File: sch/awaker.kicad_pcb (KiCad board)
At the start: 2 copper layers, 35 parts, among them P1 CONN_01X03, P2 CONN_01X07, P3 uart, P4 swd, P5 CONN_01X06, P6 speaker, P7 pow_led, P8 power, P9 CONN_01X07, Q1 Q_NMOS_GDS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

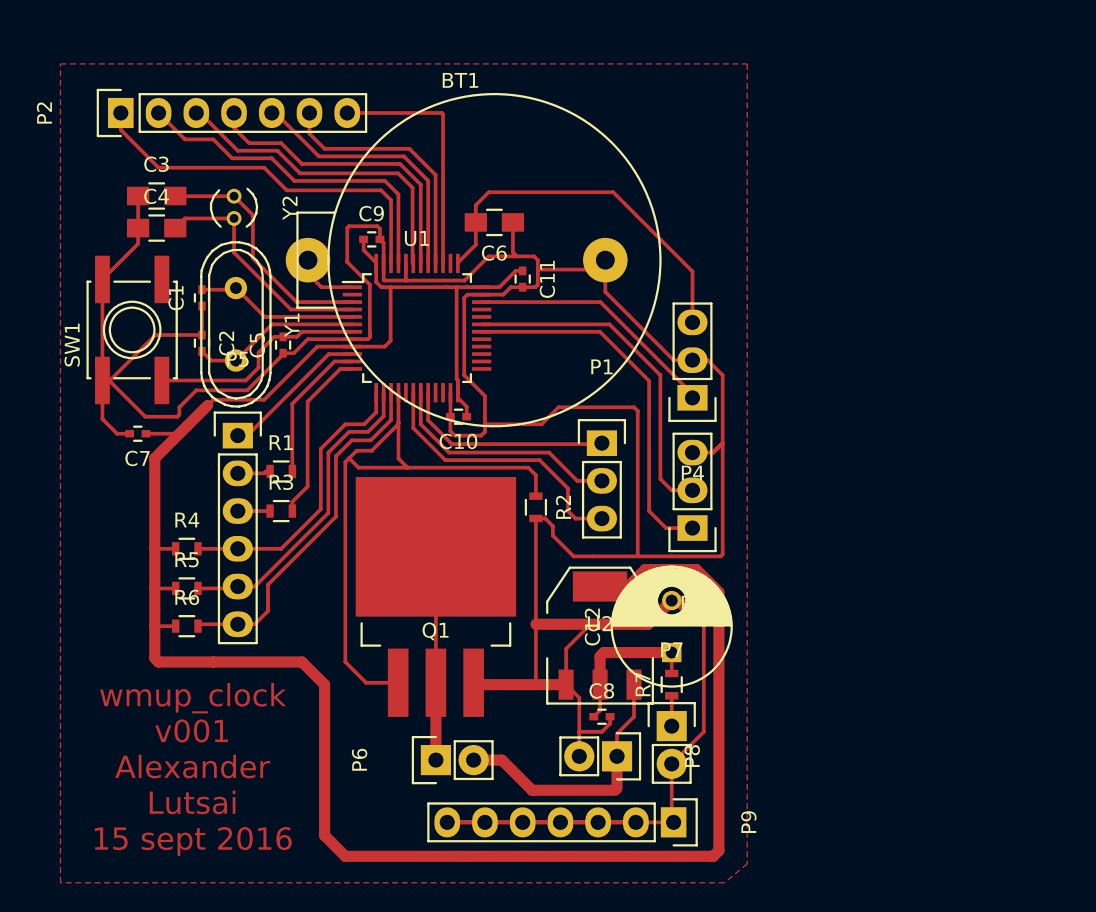
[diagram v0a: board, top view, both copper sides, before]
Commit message: reset. New board.
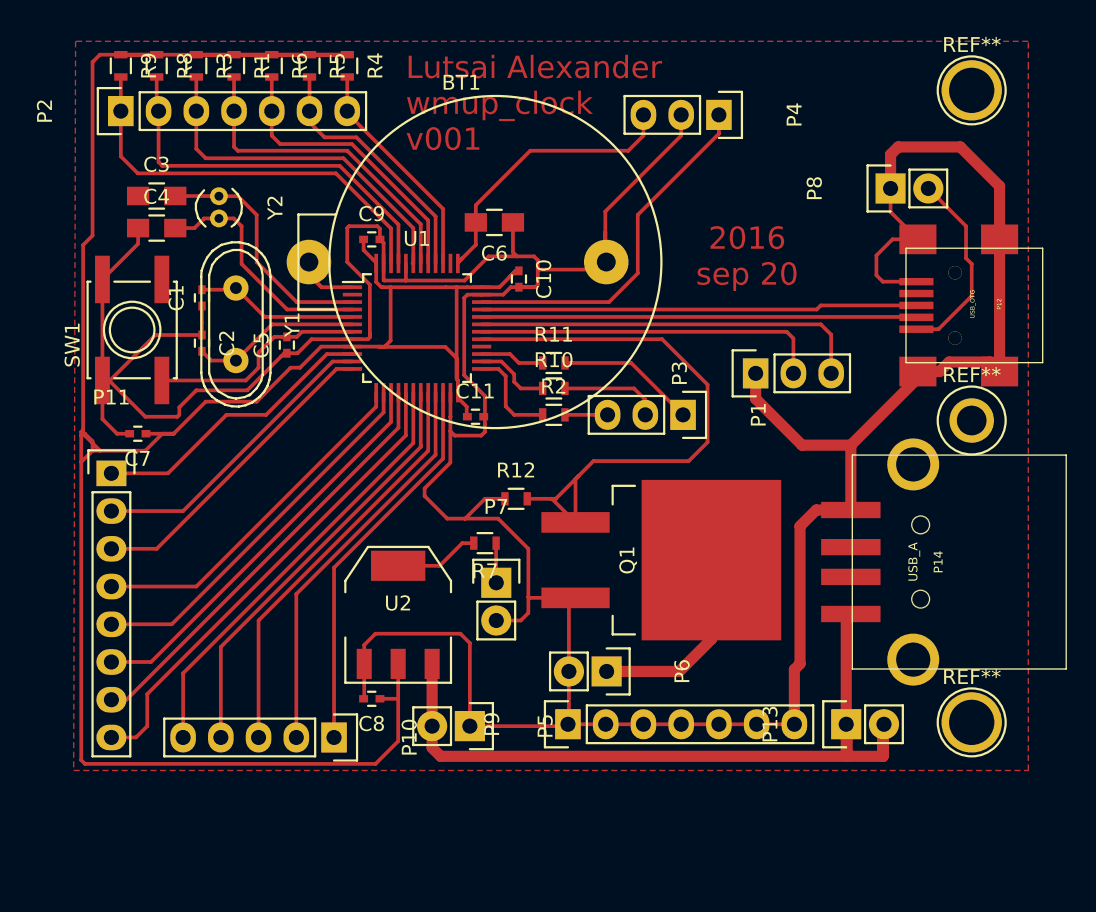
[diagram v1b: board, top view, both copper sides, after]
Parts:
- removed C12: 2200uF, Capacitors_ThroughHole:C_Radial_D8_L11.5_P3.5
- added P10: CONN_01X05, Pin_Headers:Pin_Header_Straight_1x05, F.Cu at (145.0, 137.5)
- added P11: CONN_01X08, Pin_Headers:Pin_Header_Straight_1x08, F.Cu at (130.0, 119.8)
- added P12: USB_OTG, kicad-libraries1:USB-MINI-B-SMD, F.Cu at (192.1, 108.5)
- added P13: usb_power, Pin_Headers:Pin_Header_Straight_1x02, F.Cu at (179.5, 136.7)
- added P14: USB_A, kicad-libraries1:USB-A-SMT-8231-PEG, F.Cu at (184.0, 125.7)
- added R10: 330, Resistors_SMD:R_0603, F.Cu at (159.8, 114.0)
- added R11: 330, Resistors_SMD:R_0603, F.Cu at (159.8, 112.3)
- added R12: 10k, Resistors_SMD:R_0603, F.Cu at (157.3, 121.5)
- added R8: 10k, Resistors_SMD:R_0603, F.Cu at (133.1, 92.3)
- added R9: 10k, Resistors_SMD:R_0603, F.Cu at (130.7, 92.3)
- added REF**: 1pin, Connect:1pin, F.Cu at (188.0, 136.5)
- added REF**: 1pin, Connect:1pin, F.Cu at (188.0, 94.0)
- added REF**: 1pin, Connect:1pin, F.Cu at (188.0, 116.2)
- P5: value CONN_01X06 -> power; footprint Pin_Headers:Pin_Header_Straight_1x06 -> Pin_Headers:Pin_Header_Straight_1x02
- P8: value power -> usb
- R1, R3: value 330 -> 10k
- R2: value R_Small -> 330
- U1: value STM32F100C4 -> STM32F103CB
- moved P8 42.4 mm to (182.5, 100.6), turned to 90 degrees
- moved R6 38.1 mm to (140.8, 92.3), turned to 270 degrees
- moved R5 36.1 mm to (143.4, 92.3), turned to 270 degrees
- moved R4 34.3 mm to (145.9, 92.3), turned to 270 degrees
- moved R3 30.5 mm to (135.8, 92.3), turned to 270 degrees
- moved R1 27.5 mm to (138.3, 92.3), turned to 270 degrees
- moved P5 25.0 mm to (154.2, 136.8), turned to 270 degrees
- moved P4 19.1 mm to (170.9, 95.6), turned to 270 degrees
- moved R7 15.8 mm to (155.2, 124.5), turned to 180 degrees
- moved C8 15.5 mm to (147.6, 134.9), turned to 180 degrees
- moved P7 15.3 mm to (156.0, 127.1)
- moved U2 13.7 mm to (149.4, 129.3)
- moved P6 13.0 mm to (163.4, 133.1), turned to 270 degrees
- moved Q1 12.5 mm to (161.3, 125.6), turned to 0 degrees
- moved P3 11.2 mm to (173.4, 113.0), turned to 90 degrees
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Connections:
- P3 pad 1: Net-(P3-Pad1) -> GND
- P3 pad 3: GND -> Net-(P3-Pad3)
- P5 pad 1: Net-(P5-Pad1) -> GND
- P5 pad 2: Net-(P5-Pad2) -> +5V
- P6 pad 2: Net-(P6-Pad2) -> GND
- P8 pad 1: Net-(P6-Pad2) -> GND
- P8 pad 2: GND -> Net-(P12-Pad1)
- R1 pad 1: Net-(P5-Pad2) -> +3V3
- R1 pad 2: Net-(R1-Pad2) -> Net-(P2-Pad4)
- R2 pad 1: Net-(Q1-Pad1) -> Net-(R2-Pad1)
- R2 pad 2: GND -> Net-(P1-Pad3)
- R3 pad 1: Net-(P5-Pad3) -> +3V3
- R3 pad 2: Net-(R3-Pad2) -> Net-(P2-Pad3)
- R4 pad 2: Net-(P5-Pad4) -> Net-(P2-Pad7)
- R5 pad 2: Net-(P5-Pad5) -> Net-(P2-Pad6)
- R6 pad 2: Net-(P5-Pad6) -> Net-(P2-Pad5)
- U1 pad 10: Net-(P5-Pad1) -> Net-(P11-Pad1)
- U1 pad 11: Net-(R1-Pad2) -> Net-(P11-Pad2)
- U1 pad 12: Net-(R3-Pad2) -> Net-(P11-Pad3)
- U1 pad 13: Net-(P5-Pad4) -> Net-(P11-Pad4)
- U1 pad 14: Net-(P5-Pad5) -> Net-(P11-Pad5)
- U1 pad 15: Net-(P5-Pad6) -> Net-(P11-Pad6)
- U1 pad 16: Net-(Q1-Pad1) -> Net-(P11-Pad7)
- U1 pad 18: Net-(P1-Pad3) -> Net-(P10-Pad5)
- U1 pad 19: Net-(P1-Pad2) -> Net-(P10-Pad4)
- U1 pad 20: Net-(P1-Pad1) -> Net-(P10-Pad3)
- U1 pad 25: Net-(U1-Pad25) -> Net-(R2-Pad1)
- U1 pad 29: Net-(U1-Pad29) -> Net-(Q1-Pad1)
- U1 pad 30: Net-(P3-Pad1) -> Net-(P3-Pad2)
- U1 pad 31: Net-(P3-Pad2) -> Net-(P3-Pad3)
- U2 pad 3: Net-(P6-Pad2) -> +5V
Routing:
- net +5V: track 0.00 -> 52.6 mm
- net Net-(P11-Pad8): track 0.00 -> 32.4 mm
- net Net-(P10-Pad5): track 0.00 -> 29.6 mm
- net Net-(P12-Pad3): track 0.00 -> 29.4 mm
- net Net-(P12-Pad2): track 0.00 -> 29.3 mm
- net Net-(P11-Pad7): track 0.00 -> 29.3 mm
- net Net-(P10-Pad4): track 0.00 -> 28.8 mm
- net Net-(P10-Pad3): track 0.00 -> 27.9 mm
- net Net-(P11-Pad6): track 0.00 -> 27.5 mm
- net Net-(P10-Pad2): track 0.00 -> 27.1 mm
- net Net-(P3-Pad3): track 0.00 -> 26.4 mm
- net Net-(P10-Pad1): track 0.00 -> 26.2 mm
- net Net-(P11-Pad5): track 0.00 -> 25.6 mm
- net Net-(P3-Pad1): track 24.8 -> 0.00 mm
- net Net-(P5-Pad6): track 24.0 -> 0.00 mm
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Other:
- board text added: "2016 sep 20"
- board text added: "Lutsai Alexander wmup_clock v001"
- board text removed: "wmup_clock v001 Alexander Lutsai 15 sept 2016"
